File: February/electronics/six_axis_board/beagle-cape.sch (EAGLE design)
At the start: 61 parts, among them IC1 74HCT244DW, IC2 74HCT244DW, IC3 74HCT244DW

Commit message: added 24V->5V converter, brake circuit
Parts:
- added C10: 22uF, rcl:CPOL-USSANYO_SMD_E7
- added C11: 220uF, rcl:CPOL-USSANYO_SMD_F8
- added D1: 1N5819, typewriter-project:1N5819
- added IC4: LM2574M-5.0, linear:LM2574M-5.0
- added L1: SLF10145, typewriter-project:SLF10145
- added Q1: BSS123, transistor-small-signal:BSS123
- added R43, R44: (no value), rcl:R-US_R1206
- added U$10, U$9: PINHEAD-5MM-1X2, controller:PINHEAD-5MM-1X2
- added U$11: IRFR3806, controller:IRFR3806
- added U$8: PINHEAD-0.2IN-1X12, controller:PINHEAD-0.2IN-1X12
- C4, C5, C6: value (none) -> 2700uF
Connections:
- new net +3V3: R44.1
- new net BRAKE: Q1.G, R44.2
- new net N$19: Q1.D, R43.2, U$11.G
- new net N$7: D1.C, IC4.OUT, L1.1
- new net N$8: U$10.P$1, U$11.D
- net +24V: now also C10.+, IC4.IN, U$10.P$2, U$9.P$1
- net GND: now also C10.-, C11.-, D1.A, IC4.!ON/OFF, IC4.GND@PWR, IC4.GNDSIG, Q1.S, U$11.S, U$9.P$2
- net OUT0A: now also U$8.P$1
- net OUT0B: now also U$8.P$2
- net OUT1A: now also U$8.P$3
- net OUT1B: now also U$8.P$4
- net OUT2A: now also U$8.P$5
- net OUT2B: now also U$8.P$6
- net OUT3A: now also U$8.P$7
- net OUT3B: now also U$8.P$8
- net OUT4A: now also U$8.P$9
- net OUT4B: now also U$8.P$10
- net OUT5A: now also U$8.P$11
- net OUT5B: now also U$8.P$12
- net VCC: now also C11.+, IC4.FB, L1.2, R43.1
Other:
- note added: "Brake"
- note added: "Power supply"

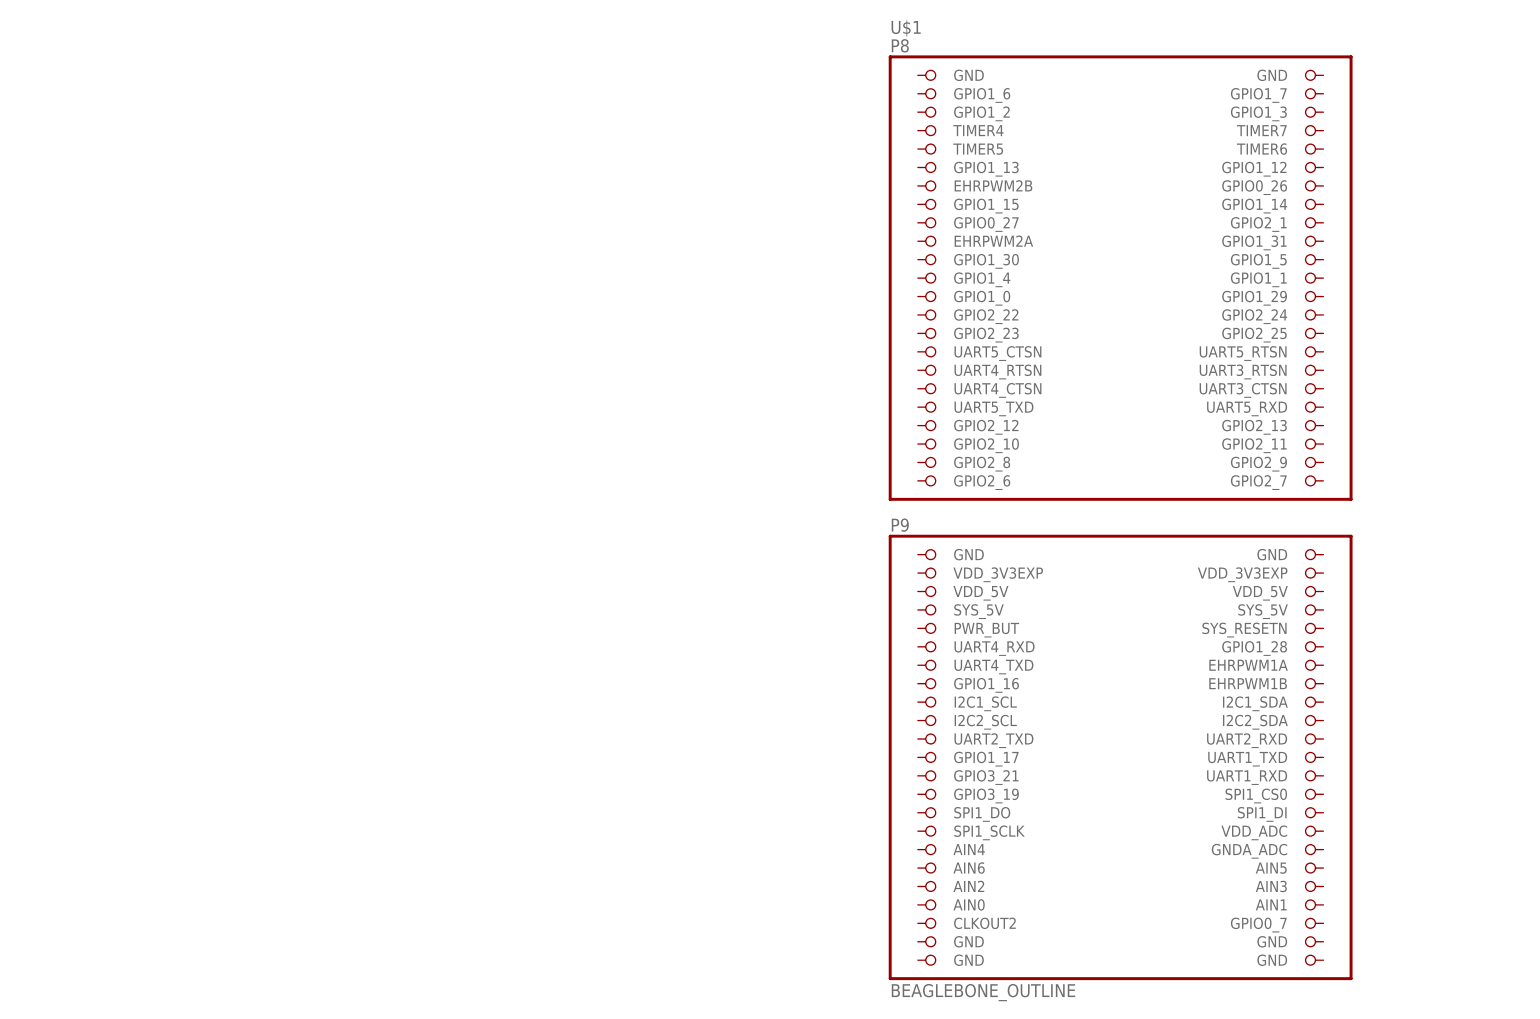
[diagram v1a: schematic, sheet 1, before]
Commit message: schematic capture complete; board time
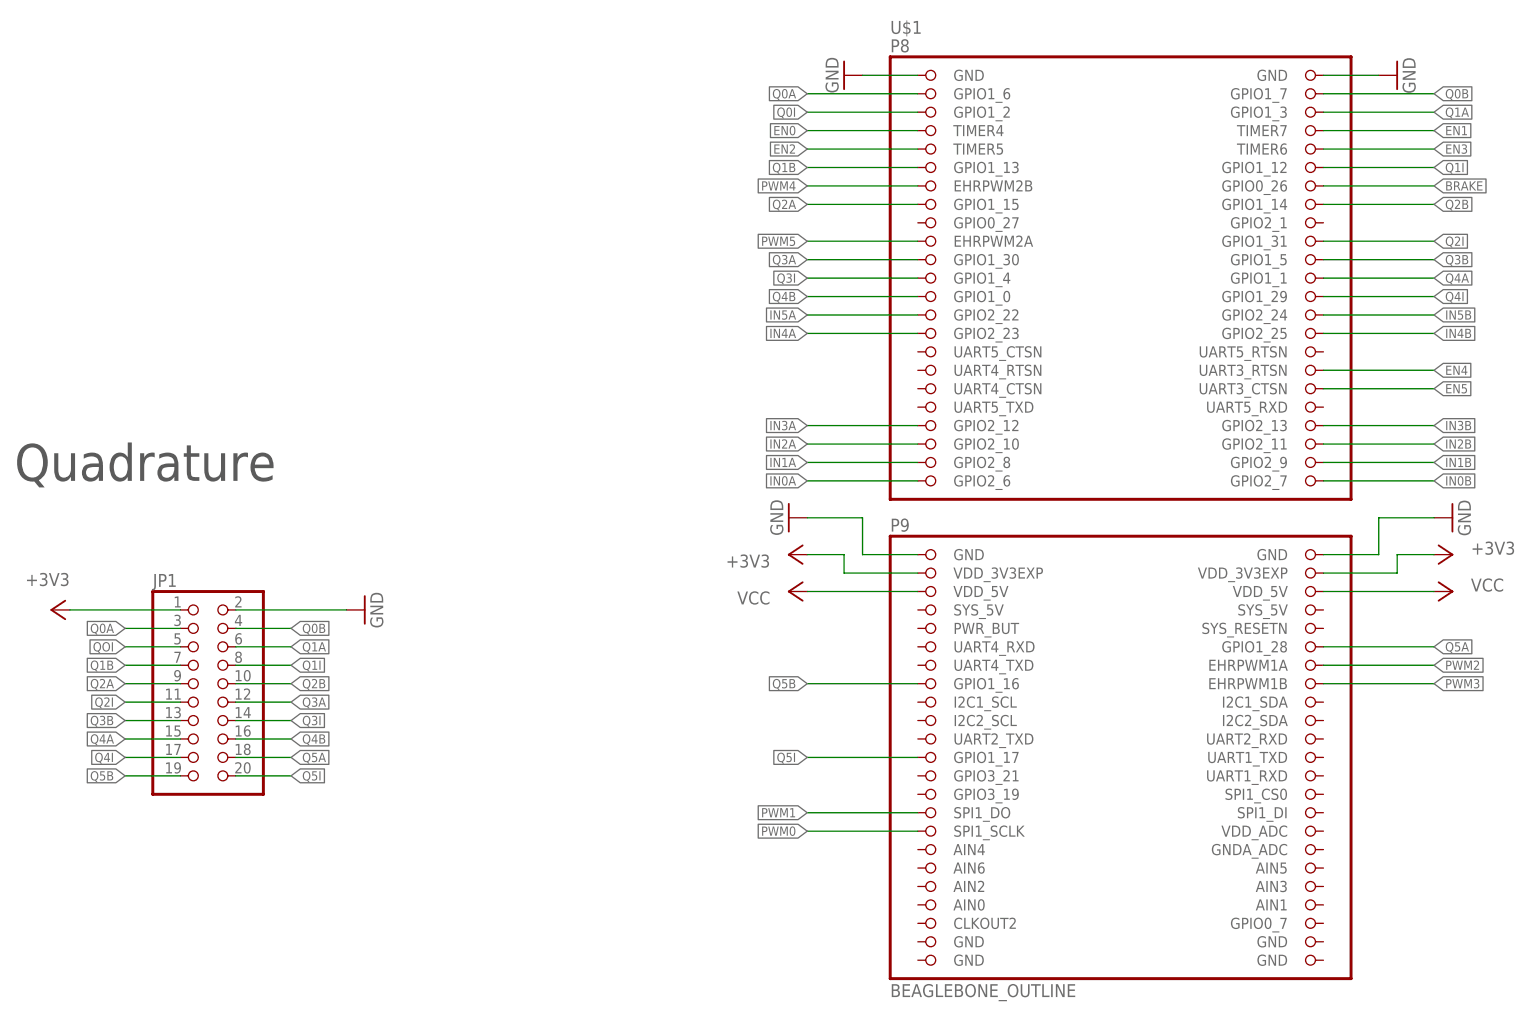
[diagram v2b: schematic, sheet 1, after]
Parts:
- added JP1: (no value), pinhead:PINHD-2X10
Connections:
- new net EN1: U$1.TIMER7
- new net EN2: U$1.TIMER5
- new net EN3: U$1.TIMER6
- new net EN4: U$1.UART3_RTSN
- new net EN5: U$1.UART3_CTSN
- new net IN1A: U$1.GPIO2_8
- new net IN1B: U$1.GPIO2_9
- new net IN2A: U$1.GPIO2_10
- new net IN2B: U$1.GPIO2_11
- new net IN3A: U$1.GPIO2_12
- new net IN3B: U$1.GPIO2_13
- new net IN4A: U$1.GPIO2_23
- new net IN4B: U$1.GPIO2_25
- new net IN5A: U$1.GPIO2_22
- new net IN5B: U$1.GPIO2_24
- new net PWM1: U$1.SPI1_DO
- new net PWM2: U$1.EHRPWM1A
- new net PWM3: U$1.EHRPWM1B
- new net PWM4: U$1.EHRPWM2B
- new net PWM5: U$1.EHRPWM2A
- new net Q0A: JP1.3, U$1.GPIO1_6
- new net Q0B: JP1.4, U$1.GPIO1_7
- new net Q0I: U$1.GPIO1_2
- new net Q1A: JP1.6, U$1.GPIO1_3
- new net Q1B: JP1.7, U$1.GPIO1_13
- new net Q1I: JP1.8, U$1.GPIO1_12
- new net Q2A: JP1.9, U$1.GPIO1_15
- new net Q2B: JP1.10, U$1.GPIO1_14
- new net Q2I: JP1.11, U$1.GPIO1_31
- new net Q3A: JP1.12, U$1.GPIO1_30
- new net Q3B: JP1.13, U$1.GPIO1_5
- new net Q3I: JP1.14, U$1.GPIO1_4
- new net Q4A: JP1.15, U$1.GPIO1_1
- new net Q4B: JP1.16, U$1.GPIO1_0
- new net Q4I: JP1.17, U$1.GPIO1_29
- new net Q5A: JP1.18, U$1.GPIO1_28
- new net Q5B: JP1.19, U$1.GPIO1_16
- new net Q5I: JP1.20, U$1.GPIO1_17
- new net QOI: JP1.5
- net +3V3: now also JP1.1, U$1.VDD_3V3EXP@1, U$1.VDD_3V3EXP@2
- net BRAKE: now also U$1.GPIO0_26
- net EN0: now also U$1.TIMER4
- net GND: now also JP1.2, U$1.GND@1, U$1.GND@2, U$1.GND@7, U$1.GND@8
- net IN0A: now also U$1.GPIO2_6
- net IN0B: now also U$1.GPIO2_7
- net PWM0: now also U$1.SPI1_SCLK
- net VCC: now also U$1.VDD_5V@1, U$1.VDD_5V@2
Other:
- note added: "Quadrature"

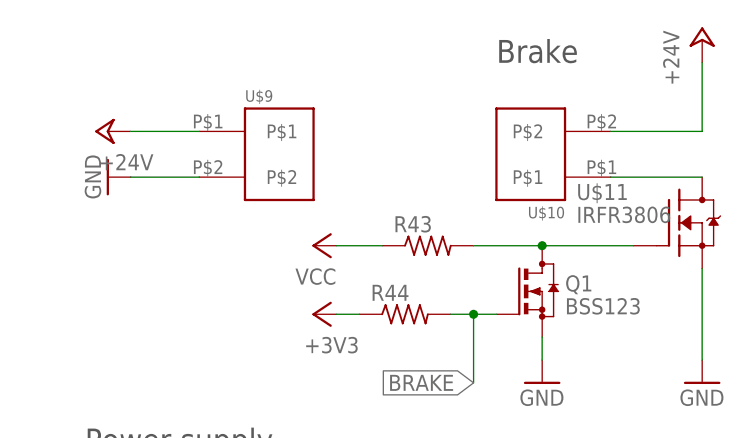
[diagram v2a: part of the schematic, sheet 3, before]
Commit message: initially laying out by hand
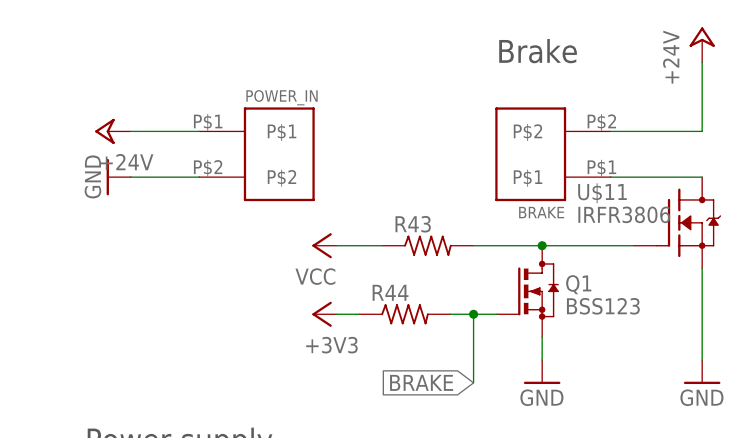
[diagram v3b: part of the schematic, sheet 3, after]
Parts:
- U$1: device adafruit:BEAGLEBONE_OUTLINE -> controller:BEAGLEBONE_OUTLINE
- renumbered U$10 to BRAKE, U$9 to POWER_IN
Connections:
- removed net QOI: JP1.5
- new net N$20: R39.2, U$7.IN_B
- new net N$21: R38.2, U$7.PWM
- new net N$22: R37.2, U$7.IN_A
- new net N$23: R40.2, U$7.DIAG_EN_B
- new net N$30: R12.2, U$3.DIAG_EN_B
- new net N$31: R11.2, U$3.IN_B
- new net N$42: R10.2, U$3.PWM
- new net N$43: R9.2, U$3.IN_A
- new net N$50: R26.2, U$5.DIAG_EN_B
- new net N$51: R25.2, U$5.IN_B
- new net N$62: R24.2, U$5.PWM
- new net N$63: R23.2, U$5.IN_A
- net EN1: now also IC1B.A1
- net EN2: now also IC2A.A1
- net EN3: now also IC2B.A1
- net EN4: now also IC3A.A1
- net EN5: now also IC3B.A1
- net IN1A: now also IC1B.A2
- net IN1B: now also IC1B.A4
- net IN2A: now also IC2A.A2
- net IN2B: now also IC2A.A4
- net IN3A: now also IC2B.A2
- net IN3B: now also IC2B.A4
- net IN4A: now also IC3A.A2
- net IN4B: now also IC3A.A4
- net IN5A: now also IC3B.A2
- net IN5B: now also IC3B.A4
- net PWM1: now also IC1B.A3
- net PWM2: now also IC2A.A3
- net PWM3: now also IC2B.A3
- net PWM4: now also IC3A.A3
- net PWM5: now also IC3B.A3
- net Q0I: now also JP1.5
